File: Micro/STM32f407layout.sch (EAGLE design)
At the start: 68 parts, among them Q1 ASF, Q2 ASV-8, T3 FDN340P, T4 AP1117_LIN_REG

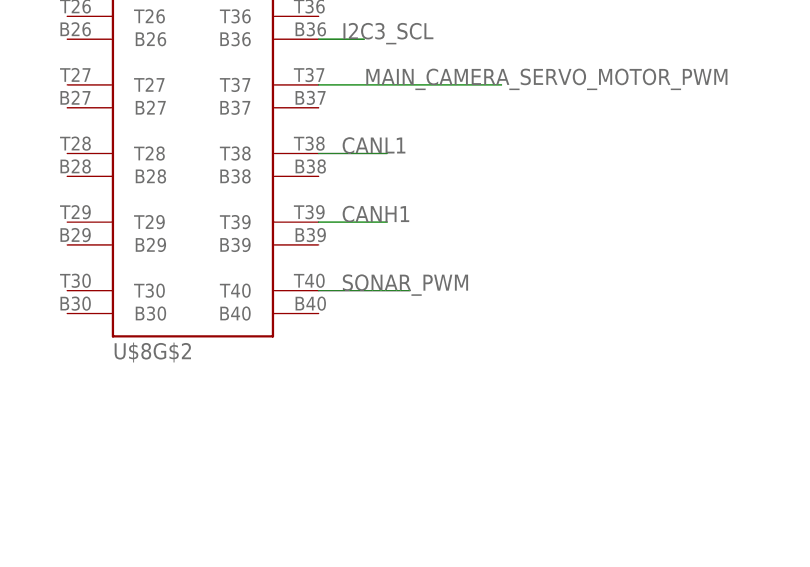
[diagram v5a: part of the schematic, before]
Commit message: Cleaned up the board
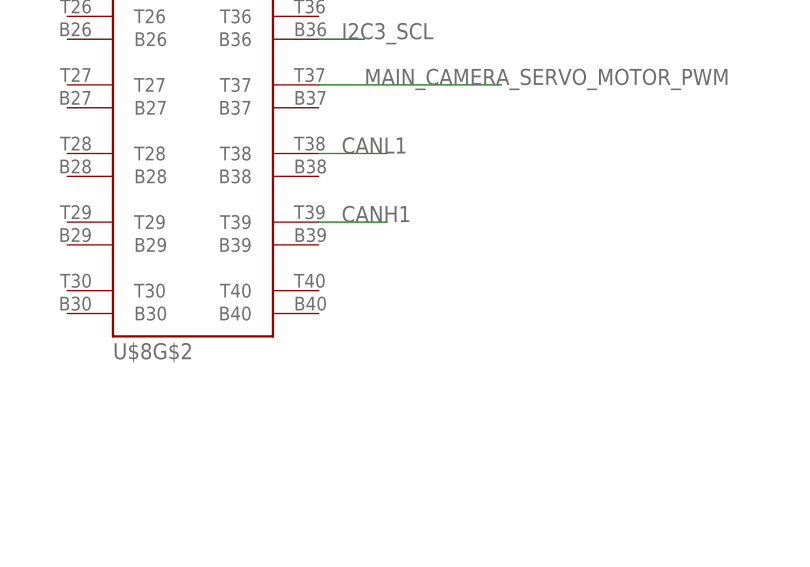
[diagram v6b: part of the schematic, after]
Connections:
- net SONAR_PWM: no longer U$8G$2.T40
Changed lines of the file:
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@@
 <?xml version="1.0" encoding="utf-8"?>
 <!DOCTYPE eagle SYSTEM "eagle.dtd">
-<eagle version="7.5.0">
+<eagle version="7.2.0">
 <drawing>
 <settings>
@@
 <label x="576.58" y="147.32" size="1.778" layer="95"/>
 </segment>
-<segment>
-<pinref part="U$8" gate="G$2" pin="T40"/>
-<wire x1="571.5" y1="101.6" x2="581.66" y2="101.6" width="0.1524" layer="91"/>
-<label x="574.04" y="101.6" size="1.778" layer="95"/>
-</segment>
 </net>

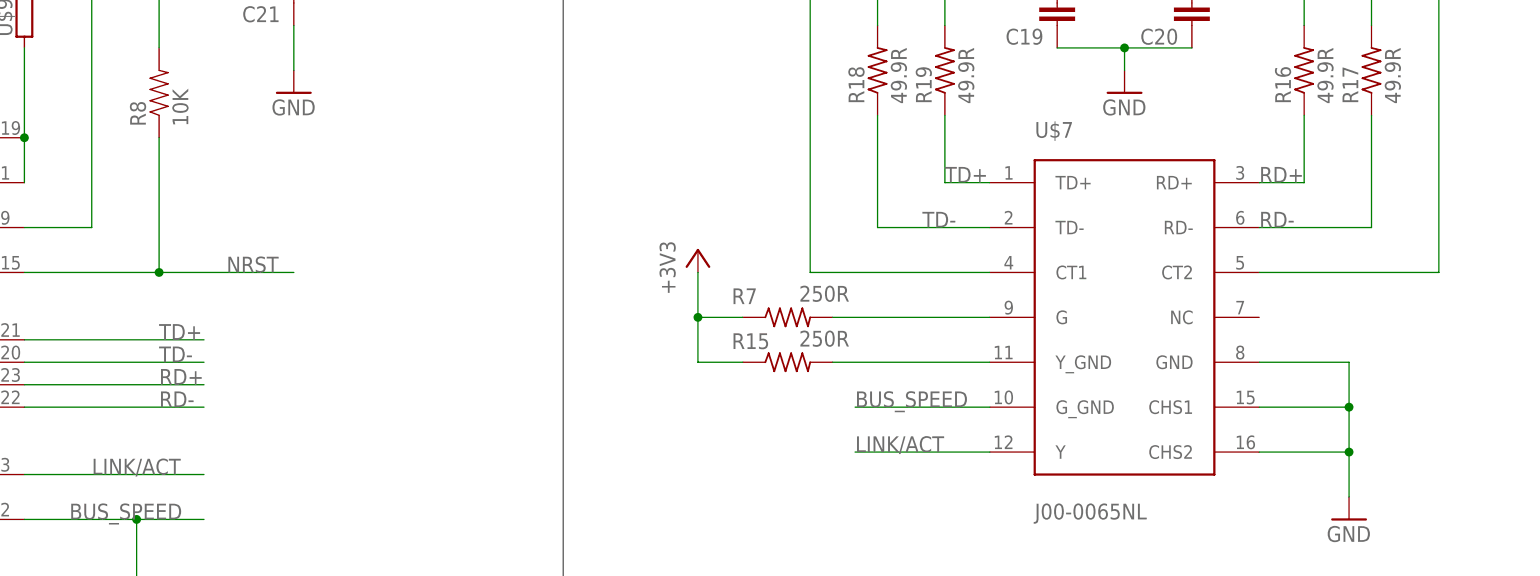
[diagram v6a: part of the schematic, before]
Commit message: Update to fix information from "final" design review
moved micro usb connector, fixed power square
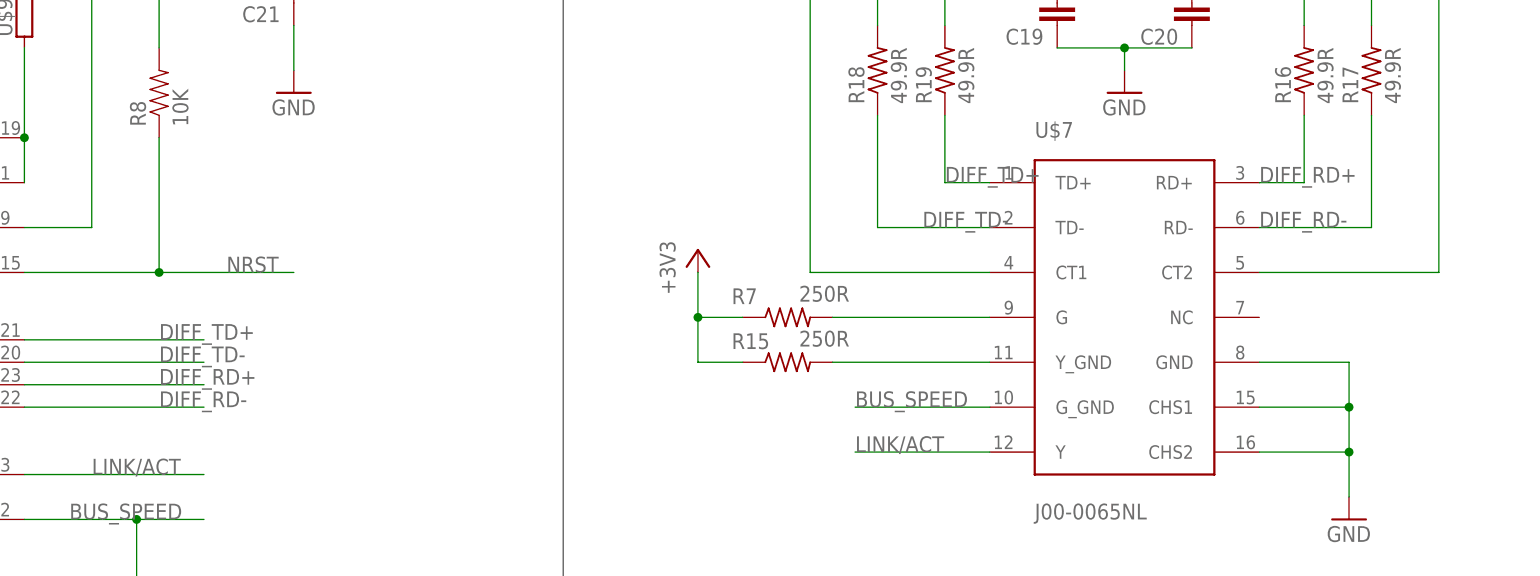
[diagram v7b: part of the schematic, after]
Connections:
- net RD+ renamed DIFF_RD+
- net RD- renamed DIFF_RD-
- net TD+ renamed DIFF_TD+
- net TD- renamed DIFF_TD-
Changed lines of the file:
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@@
 <?xml version="1.0" encoding="utf-8"?>
 <!DOCTYPE eagle SYSTEM "eagle.dtd">
-<eagle version="7.2.0">
+<eagle version="7.5.0">
 <drawing>
 <settings>
@@
 <classes>
 <class number="0" name="default" width="0" drill="0">
+</class>
+<class number="1" name="DiffPair" width="0.254" drill="0">
 </class>
 </classes>
@@
 </segment>
 </net>
-<net name="TD+" class="0">
+<net name="DIFF_TD+" class="1">
 <segment>
 <wire x1="1008.38" y1="165.1" x2="1003.3" y2="165.1" width="0.1524" layer="91"/>
@@
 </segment>
 </net>
-<net name="RD+" class="0">
+<net name="DIFF_RD+" class="1">
 <segment>
 <wire x1="1038.86" y1="165.1" x2="1043.94" y2="165.1" width="0.1524" layer="91"/>
@@
 </segment>
 </net>
-<net name="RD-" class="0">
+<net name="DIFF_RD-" class="1">
 <segment>
 <label x="1038.86" y="160.02" size="1.778" layer="95"/>
@@
 </segment>
 </net>
-<net name="TD-" class="0">
+<net name="DIFF_TD-" class="1">
 <segment>
 <pinref part="U$4" gate="G$1" pin="TXN"/>

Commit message: Finished changes for trying to fix micro board
Last push of integrated ethernet
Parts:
- added Q3: ASF, DiscreteComponents:ASF
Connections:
- new net N$28: Q3.FO, Q3.GND, Q3.OE, Q3.VCC
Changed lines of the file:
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@@
 <part name="U$8" library="Connectors" deviceset="HSC8PART-60" device=""/>
 <part name="P+1" library="supply1" deviceset="+5V" device=""/>
+<part name="Q3" library="DiscreteComponents" deviceset="ASF*" device=""/>
 </parts>
 <sheets>
@@
 <instance part="U$8" gate="G$3" x="683.26" y="134.62"/>
 <instance part="P+1" gate="1" x="441.96" y="147.32"/>
+<instance part="Q3" gate="G$1" x="53.34" y="167.64"/>
 </instances>
 <busses>
@@
 </segment>
 </net>
+<net name="N$28" class="0">
+<segment>
+<pinref part="Q3" gate="G$1" pin="OE"/>
+<pinref part="Q3" gate="G$1" pin="FO"/>
+<wire x1="66.04" y1="172.72" x2="66.04" y2="167.64" width="0.1524" layer="91"/>
+<wire x1="66.04" y1="167.64" x2="66.04" y2="154.94" width="0.1524" layer="91"/>
+<junction x="66.04" y="167.64"/>
+<wire x1="66.04" y1="154.94" x2="40.64" y2="154.94" width="0.1524" layer="91"/>
+<pinref part="Q3" gate="G$1" pin="VCC"/>
+<pinref part="Q3" gate="G$1" pin="GND"/>
+<wire x1="40.64" y1="172.72" x2="40.64" y2="162.56" width="0.1524" layer="91"/>
+<wire x1="40.64" y1="154.94" x2="40.64" y2="162.56" width="0.1524" layer="91"/>
+<junction x="40.64" y="162.56"/>
+</segment>
+</net>
